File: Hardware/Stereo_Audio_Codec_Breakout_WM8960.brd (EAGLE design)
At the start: 25.4 x 40.6 mm, 146 parts, among them J1 QWIIC, U3 XC6222B331MR-G, U4 WM8960, Y1 24 MHz

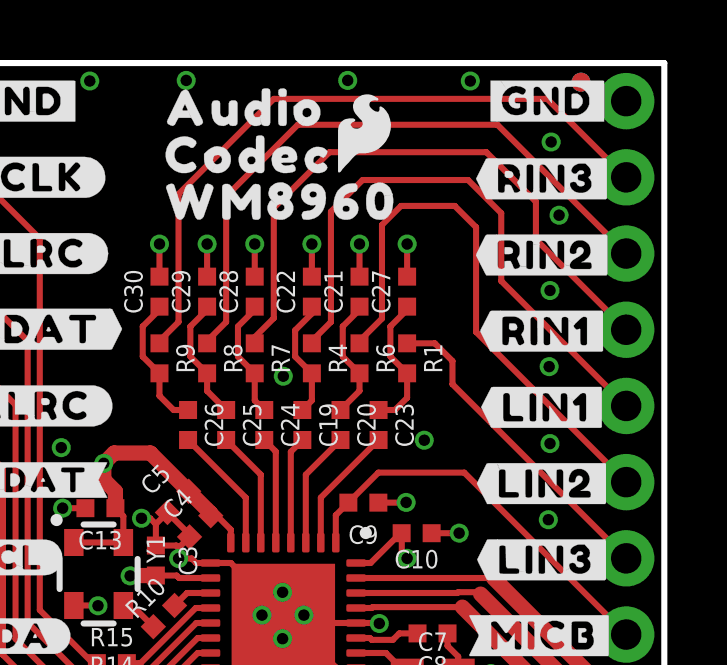
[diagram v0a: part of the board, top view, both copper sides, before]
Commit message: Moved fiducials to avoid silk overlap
-also increase I2C address text size in sch
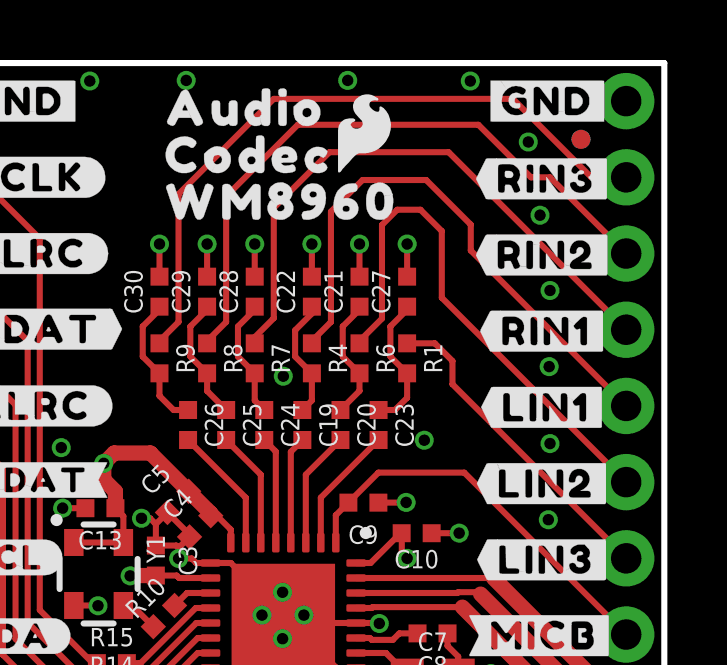
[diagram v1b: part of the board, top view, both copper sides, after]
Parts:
- moved FD3 1.91 mm to (22.6, 38.1)
- moved FD4 1.91 mm to (22.6, 38.1)
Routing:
- net LINPUT2: track 18.5 -> 17.7 mm
- net LINPUT1: track 19.4 -> 18.6 mm
- net RINPUT1: track 20.5 -> 19.7 mm
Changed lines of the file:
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@@
 <setting verticaltext="up"/>
 </settings>
-<grid distance="0.05" unitdist="inch" unit="inch" style="lines" multiple="1" display="yes" altdistance="0.0001" altunitdist="inch" altunit="inch"/>
+<grid distance="0.05" unitdist="inch" unit="inch" style="lines" multiple="1" display="yes" altdistance="0.005" altunitdist="inch" altunit="inch"/>
 <layers>
 <layer number="1" name="Top" color="4" fill="1" visible="yes" active="yes"/>
@@
 <element name="FD1" library="SparkFun-Aesthetics" package="FIDUCIAL-MICRO" value="FIDUCIALUFIDUCIAL" x="2.078740625" y="2.5357" smashed="yes"/>
 <element name="FD2" library="SparkFun-Aesthetics" package="FIDUCIAL-MICRO" value="FIDUCIALUFIDUCIAL" x="2.078740625" y="2.5357" smashed="yes" rot="MR0"/>
-<element name="FD3" library="SparkFun-Aesthetics" package="FIDUCIAL-MICRO" value="FIDUCIALUFIDUCIAL" x="22.6226" y="40.0021" smashed="yes" rot="R180"/>
-<element name="FD4" library="SparkFun-Aesthetics" package="FIDUCIAL-MICRO" value="FIDUCIALUFIDUCIAL" x="22.6226" y="40.0021" smashed="yes" rot="MR180"/>
+<element name="FD3" library="SparkFun-Aesthetics" package="FIDUCIAL-MICRO" value="FIDUCIALUFIDUCIAL" x="22.6226" y="38.0971" smashed="yes" rot="R180"/>
+<element name="FD4" library="SparkFun-Aesthetics" package="FIDUCIAL-MICRO" value="FIDUCIALUFIDUCIAL" x="22.6226" y="38.0971" smashed="yes" rot="MR180"/>
 <element name="Y1" library="SparkFun-Clocks" package="RESONATOR-SMD-3.2X2.5" value="24 MHz" x="6.5433" y="23.6085" smashed="yes" rot="R270">
 <attribute name="NAME" x="8.1433" y="24.9085" size="0.6096" layer="25" font="vector" ratio="20" rot="R270"/>
@@
 <contactref element="R7" pad="1"/>
 <contactref element="J5" pad="13"/>
-<wire x1="24.13" y1="31.75" x2="21.1201" y2="34.7599" width="0.2032" layer="1"/>
-<wire x1="21.1201" y1="36.0172" x2="19.4691" y2="37.6682" width="0.2032" layer="1"/>
-<wire x1="19.4691" y1="37.6682" x2="14.2367" y2="37.6682" width="0.2032" layer="1"/>
+<wire x1="24.13" y1="31.75" x2="18.2118" y2="37.6682" width="0.2032" layer="1"/>
+<wire x1="18.2118" y1="37.6682" x2="14.2367" y2="37.6682" width="0.2032" layer="1"/>
 <wire x1="12.3825" y1="32.1357" x2="11.7475" y2="31.5007" width="0.2032" layer="1"/>
 <wire x1="11.7475" y1="31.5007" x2="11.7475" y2="31.2975" width="0.2032" layer="1"/>
-<wire x1="21.1201" y1="34.7599" x2="21.1201" y2="36.0172" width="0.2032" layer="1"/>
 <wire x1="14.2367" y1="37.6682" x2="12.3825" y2="35.814" width="0.2032" layer="1"/>
 <wire x1="12.3825" y1="35.814" x2="12.3825" y2="32.1357" width="0.2032" layer="1"/>
@@
 <contactref element="R4" pad="1"/>
 <contactref element="J5" pad="12"/>
-<wire x1="24.13" y1="29.21" x2="19.9644" y2="33.3756" width="0.2032" layer="1"/>
-<wire x1="19.9644" y1="35.6362" x2="18.8595" y2="36.7411" width="0.2032" layer="1"/>
-<wire x1="18.8595" y1="36.7411" x2="15.3416" y2="36.7411" width="0.2032" layer="1"/>
+<wire x1="24.13" y1="29.21" x2="18.9484" y2="34.3916" width="0.2032" layer="1"/>
+<wire x1="18.9484" y1="35.2552" x2="17.4625" y2="36.7411" width="0.2032" layer="1"/>
+<wire x1="17.4625" y1="36.7411" x2="15.3416" y2="36.7411" width="0.2032" layer="1"/>
 <wire x1="15.3416" y1="36.7411" x2="14.2875" y2="35.687" width="0.2032" layer="1"/>
 <wire x1="14.2875" y1="32.0087" x2="13.6525" y2="31.3737" width="0.2032" layer="1"/>
 <wire x1="13.6525" y1="31.3737" x2="13.6525" y2="31.2975" width="0.2032" layer="1"/>
-<wire x1="19.9644" y1="33.3756" x2="19.9644" y2="35.6362" width="0.2032" layer="1"/>
+<wire x1="18.9484" y1="34.3916" x2="18.9484" y2="35.2552" width="0.2032" layer="1"/>
 <wire x1="14.2875" y1="35.687" x2="14.2875" y2="32.0087" width="0.2032" layer="1"/>
 </signal>
@@
 <contactref element="R9" pad="1"/>
 <contactref element="J5" pad="15"/>
-<wire x1="24.13" y1="36.83" x2="24.112221875" y2="36.83" width="0.2032" layer="1"/>
-<wire x1="24.112221875" y1="36.83" x2="21.496021875" y2="39.4462" width="0.2032" layer="1"/>
-<wire x1="21.496021875" y1="39.4462" x2="12.3825" y2="39.4462" width="0.2032" layer="1"/>
+<wire x1="24.13" y1="36.83" x2="22.969221875" y2="36.83" width="0.2032" layer="1"/>
+<wire x1="22.969221875" y1="36.83" x2="20.353021875" y2="39.4462" width="0.2032" layer="1"/>
+<wire x1="20.353021875" y1="39.4462" x2="12.3825" y2="39.4462" width="0.2032" layer="1"/>
 <wire x1="12.3825" y1="39.4462" x2="9.2075" y2="36.2712" width="0.2032" layer="1"/>
 <wire x1="9.2075" y1="32.0087" x2="8.5725" y2="31.3737" width="0.2032" layer="1"/>
@@
 <contactref element="R8" pad="1"/>
 <contactref element="J5" pad="14"/>
-<wire x1="24.13" y1="34.29" x2="19.8374" y2="38.5826" width="0.2032" layer="1"/>
+<wire x1="24.13" y1="34.29" x2="21.59" y2="36.83" width="0.2032" layer="1"/>
+<wire x1="21.59" y1="36.83" x2="20.955" y2="36.83" width="0.2032" layer="1"/>
+<wire x1="20.955" y1="36.83" x2="19.2024" y2="38.5826" width="0.2032" layer="1"/>
 <wire x1="13.1826" y1="38.5826" x2="10.795" y2="36.195" width="0.2032" layer="1"/>
 <wire x1="10.795" y1="32.0087" x2="10.16" y2="31.3737" width="0.2032" layer="1"/>
 <wire x1="10.16" y1="31.3737" x2="10.16" y2="31.2975" width="0.2032" layer="1"/>
-<wire x1="19.8374" y1="38.5826" x2="13.1826" y2="38.5826" width="0.2032" layer="1"/>
+<wire x1="19.2024" y1="38.5826" x2="13.1826" y2="38.5826" width="0.2032" layer="1"/>
 <wire x1="10.795" y1="36.195" x2="10.795" y2="32.0087" width="0.2032" layer="1"/>
 </signal>
@@
 <contactref element="R6" pad="1"/>
 <contactref element="J5" pad="11"/>
-<wire x1="24.13" y1="26.67" x2="19.1262" y2="31.6738" width="0.2032" layer="1"/>
-<wire x1="19.1262" y1="35.1663" x2="18.415" y2="35.8775" width="0.2032" layer="1"/>
-<wire x1="18.415" y1="35.8775" x2="16.6243" y2="35.8775" width="0.2032" layer="1"/>
+<wire x1="24.13" y1="26.67" x2="17.9832" y2="32.8168" width="0.2032" layer="1"/>
+<wire x1="17.9832" y1="35.0393" x2="17.272" y2="35.7505" width="0.2032" layer="1"/>
+<wire x1="17.272" y1="35.7505" x2="16.4973" y2="35.7505" width="0.2032" layer="1"/>
 <wire x1="15.9893" y1="32.123" x2="15.24" y2="31.3737" width="0.2032" layer="1"/>
 <wire x1="15.24" y1="31.3737" x2="15.24" y2="31.2975" width="0.2032" layer="1"/>
-<wire x1="19.1262" y1="31.6738" x2="19.1262" y2="35.1663" width="0.2032" layer="1"/>
-<wire x1="16.6243" y1="35.8775" x2="15.9893" y2="35.2425" width="0.2032" layer="1"/>
+<wire x1="17.9832" y1="32.8168" x2="17.9832" y2="35.0393" width="0.2032" layer="1"/>
+<wire x1="16.4973" y1="35.7505" x2="15.9893" y2="35.2425" width="0.2032" layer="1"/>
 <wire x1="15.9893" y1="35.2425" x2="15.9893" y2="32.123" width="0.2032" layer="1"/>
 </signal>
@@
 <via x="21.562059375" y="30.5206375" extent="1-16" drill="0.381"/>
 <via x="21.59" y="33.058096875" extent="1-16" drill="0.381"/>
-<via x="21.892259375" y="35.56761875" extent="1-16" drill="0.381"/>
-<via x="21.628096875" y="38.008559375" extent="1-16" drill="0.381"/>
+<via x="21.257259375" y="35.56761875" extent="1-16" drill="0.381"/>
+<via x="20.866096875" y="38.008559375" extent="1-16" drill="0.381"/>
 <via x="22.84221875" y="12.669521875" extent="1-16" drill="0.381"/>
 <via x="22.908259375" y="7.6327" extent="1-16" drill="0.381"/>
